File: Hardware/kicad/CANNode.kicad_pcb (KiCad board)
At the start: 4 copper layers, 66.5 x 57 mm, 58 parts, among them J1 Conn_01x04, J11 Conn_01x04, J12 Conn_01x04, J2 Conn_01x04, J21 Conn_01x04, J31 Conn_01x04, J41 Conn_01x04, J42 Conn_01x04, J43 Conn_01x04, J44 Conn_01x04, J61 Conn_02x04_Odd_Even, J81 Conn_01x10, J91 Conn_01x04, U1 Teensy3.2, U2 SN65HVD230, U21 PCA9306, U31 MAX3485, U41 MAX3485, U91 LM1117-5.0

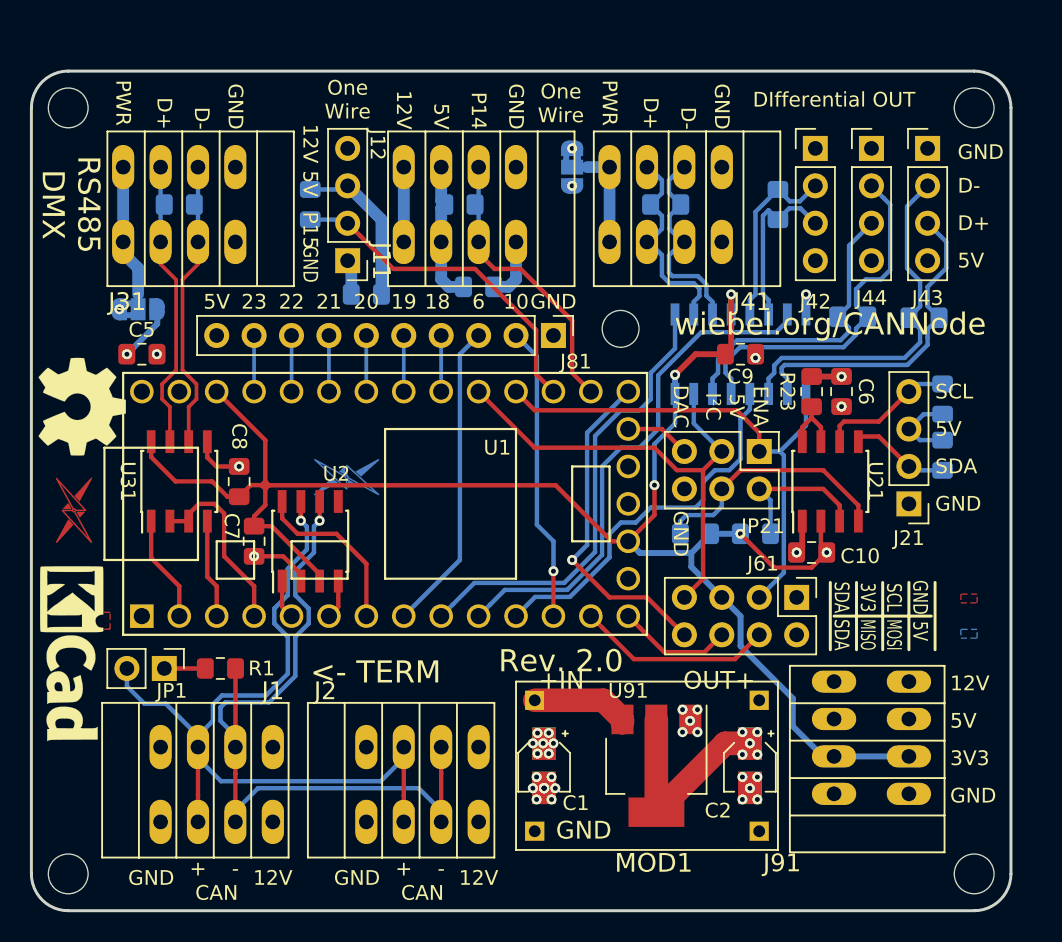
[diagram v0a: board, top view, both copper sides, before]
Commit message: second RS485 swapped with OW
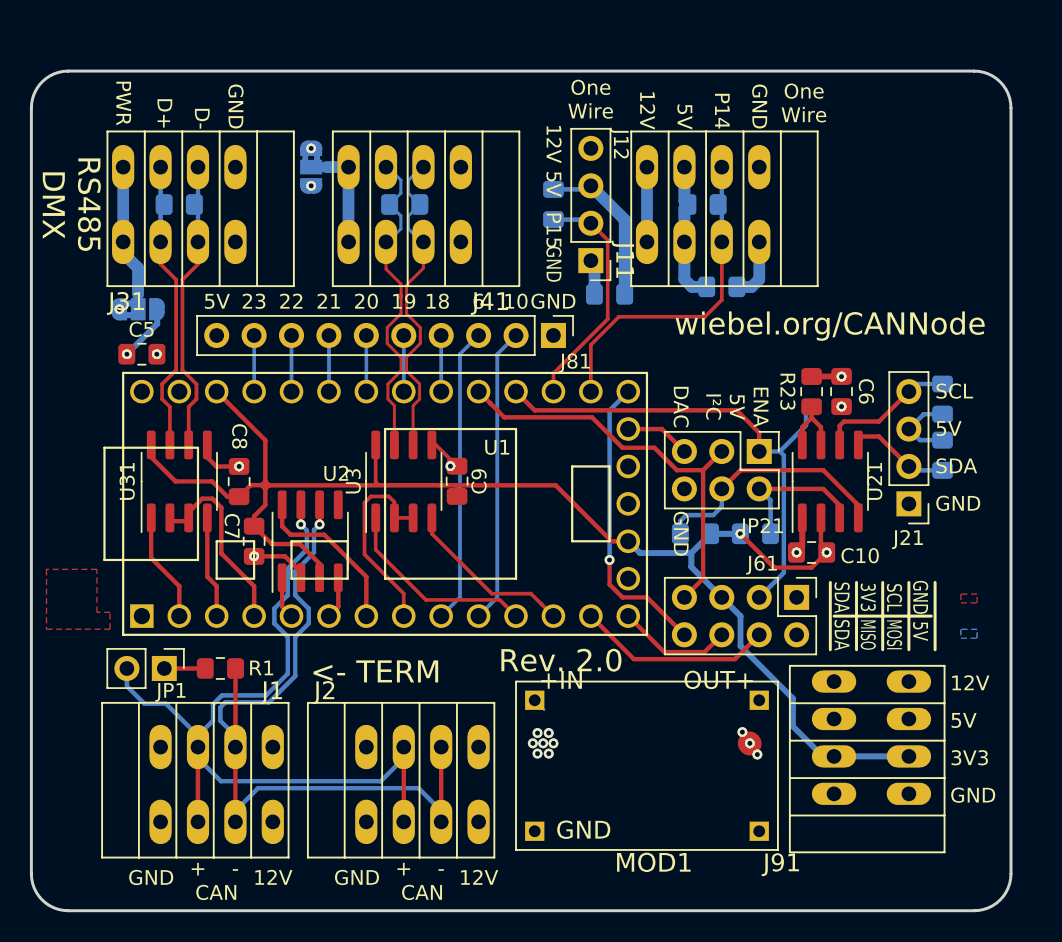
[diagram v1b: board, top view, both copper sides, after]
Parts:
- removed ? (x2): , own:LOGO_MID
- removed C1 (x2), C2 (x2): CP, Capacitor_SMD:CP_Elec_3x5.4
- removed J42, J43, J44: Conn_01x04, Connector_PinHeader_2.54mm:PinHeader_1x04_P2.54mm_Vertical
- removed R3, R4, R5: 120, Resistor_SMD:R_0805_2012Metric_Pad1.15x1.40mm_HandSolder
- removed REF** (x5): MountingHole_2.5mm, MountingHole:MountingHole_2.5mm
- removed REF**: KiCAD Logo, Symbol:Symbol_KiCAD-Logo_CopperAndSilkScreenTop
- removed REF**: OSHW-Symbol_6.7x6mm_SilkScreen, Symbol:OSHW-Symbol_6.7x6mm_SilkScreen
- removed U41: MAX3485, Package_SO:SOIC-16_3.9x9.9mm_P1.27mm
- removed U91: LM1117-5.0, Package_TO_SOT_SMD:SOT-223-3_TabPin2
- added U3: MAX3485, Package_SO:SOIC-8_3.9x4.9mm_P1.27mm, F.Cu at (94.6, 64.5)
- MOD1: value OWN_DCDC -> DSN-MINI-360
- moved C9 21.1 mm to (98.2, 64.5), turned to 90 degrees
- moved J41 17.7 mm to (90.9, 43.2)
- moved JP41 17.7 mm to (88.3, 43.2)
- moved R2 17.7 mm to (94.7, 45.7)
- moved C3 16.5 mm to (116.2, 51.3)
- moved J11 16.5 mm to (111.1, 43.2)
- moved R11 16.5 mm to (104.8, 45.7)
- moved R12 16.5 mm to (114.9, 45.7)
- moved C4 16.5 mm to (108.6, 51.8)
- moved J12 16.5 mm to (107.3, 49.5)
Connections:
- net /16 renamed /18
- net /17 renamed /19
- net /D1+ renamed /UA2+
- net /D1- renamed /UA2-
- net Net-(J12-Pad2) renamed /OW15
- J31 pad 2: /UA1+ -> /UA1-
- J31 pad 3: /UA1- -> /UA1+
- MOD1 pad IN+: +12V -> (no net)
- MOD1 pad IN-: GND -> (no net)
- MOD1 pad OUT+: +5V -> (no net)
- MOD1 pad OUT-: GND -> (no net)
- R6 pad 1: /UA1+ -> /UA1-
- R6 pad 2: /UA1- -> /UA1+
- U1 pad 10: /DI2_8 -> /10
- U1 pad 11: /EN34_9 -> Net-(U1-Pad11)
- U1 pad 12: /10 -> Net-(U1-Pad12)
- U1 pad 15: Net-(U1-Pad15) -> (no net)
- U1 pad 18: Net-(U1-Pad18) -> (no net)
- U1 pad 32: Net-(U1-Pad32) -> (no net)
- U1 pad 8: /6 -> Net-(U1-Pad8)
- U1 pad 9: /DI1_7 -> /6
- U2 pad 5: Net-(U2-Pad5) -> (no net)
- U31 pad 6: /UA1+ -> /UA1-
- U31 pad 7: /UA1- -> /UA1+
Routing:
- net /DI2_8: track 35.4 -> 0.00 mm
- net /DI1_7: track 31.4 -> 0.00 mm
- net /EN34_9: track 26.0 -> 0.00 mm
- net /D3-: track 24.9 -> 0.00 mm
- net /D4-: track 24.8 -> 0.00 mm
- net /D3+: track 22.4 -> 0.00 mm
- net /D4+: track 20.8 -> 0.00 mm
- net +5V: track 46.3 -> 31.8 mm, vias 8 -> 6
- net +3V3: track 118.5 -> 104.5 mm, vias 5 -> 2
- net Net-(U1-Pad11): track 0.00 -> 13.6 mm
- net Net-(U1-Pad8): track 0.00 -> 13.5 mm
- net /D2-: track 12.6 -> 0.00 mm
- net Net-(U1-Pad12): track 0.00 -> 11.6 mm
- net /D2+: track 11.6 -> 0.00 mm
- net /UA2+: track 14.2 -> 23.1 mm
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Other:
- board text removed: "DIfferential OUT"

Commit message: latest additions
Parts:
- moved MOD1 0.52 mm to (119.3, 89.4)
- moved C8 0.38 mm to (83.1, 64.5)
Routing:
- net Net-(U1-Pad8): track 13.5 -> 8.78 mm, vias 0 -> 1
- net +3V3: track 104.5 -> 103.4 mm
- net /UA3EN_2: track 13.0 -> 13.9 mm, vias 0 -> 1
- net /SDA0_17: track 28.4 -> 28.9 mm
- net +5V: track 31.8 -> 31.7 mm, vias 6 -> 3
- net +12V: vias 9 -> 2

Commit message: pproaching v2.5
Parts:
- removed the C5 at (76.8, 55.9)
- removed the C9 at (98.2, 64.5)
- removed J11, J91: Conn_01x04, CANNode:OWN_KF141V-P4_simple
- removed the J2 at (99.7, 87.6)
- removed J21: Conn_01x04, Connector_PinHeader_2.54mm:PinHeader_1x04_P2.54mm_Vertical
- removed JP21: Conn_02x03_Odd_Even, Connector_PinHeader_2.54mm:PinHeader_2x03_P2.54mm_Vertical
- removed R11, R12, R24, R25: 4.7k, Resistor_SMD:R_0805_2012Metric_Pad1.15x1.40mm_HandSolder
- removed the R2 at (94.7, 45.7)
- added C1: C, Capacitor_SMD:C_0805_2012Metric_Pad1.15x1.40mm_HandSolder, B.Cu at (81.2, 51.3)
- added C10: C, Capacitor_SMD:C_0805_2012Metric_Pad1.15x1.40mm_HandSolder, B.Cu at (94.6, 51.4)
- added C11: C, Capacitor_SMD:C_0805_2012Metric_Pad1.15x1.40mm_HandSolder, B.Cu at (123.8, 42.2)
- added C2: C, Capacitor_SMD:C_0805_2012Metric_Pad1.15x1.40mm_HandSolder, B.Cu at (123.8, 44.2)
- added C8: C, Capacitor_SMD:C_0805_2012Metric_Pad1.15x1.40mm_HandSolder, F.Cu at (98.3, 64.5)
- added H1: MountingHole, MountingHole:MountingHole_3.5mm, F.Cu at (72.0, 39.4)
- added H2: MountingHole, MountingHole:MountingHole_3.5mm, F.Cu at (133.2, 39.4)
- added H3: MountingHole, MountingHole:MountingHole_3.5mm, F.Cu at (72.0, 90.9)
- added H4: MountingHole, MountingHole:MountingHole_3.5mm, F.Cu at (133.2, 90.9)
- added J6: Conn_01x04, 00_mylib:WAGO_243_4-Pole, F.Cu at (131.7, 40.9)
- added J8: Conn_01x03, 00_mylib:WAGO_243_3-Pole, F.Cu at (133.7, 88.1)
- added J9: Conn_01x04, Connector_PinHeader_2.54mm:PinHeader_1x04_P2.54mm_Vertical, F.Cu at (128.9, 64.9)
- added JP4: Conn_02x03_Odd_Even, Connector_PinHeader_2.54mm:PinHeader_2x03_P2.54mm_Vertical, F.Cu at (113.7, 65.0)
- added Log1: Logo, 00_mylib:LOGO_MID, F.Cu at (73.3, 51.3)
- added Log2: Logo, Symbol:OSHW-Logo_5.7x6mm_Copper, F.Cu at (73.3, 55.6)
- added Log3: Logo, 00_mylib:LOGO_MID, B.Cu at (113.7, 55.1)
- added Log4: Logo, Symbol:OSHW-Logo_5.7x6mm_Copper, B.Cu at (105.0, 63.8)
- added R3: 120, Resistor_SMD:R_0805_2012Metric_Pad1.15x1.40mm_HandSolder, B.Cu at (94.6, 45.7)
- added R4: 4.7k, Resistor_SMD:R_0805_2012Metric_Pad1.15x1.40mm_HandSolder, B.Cu at (103.3, 45.7)
- added R5: 4.7k, Resistor_SMD:R_0805_2012Metric_Pad1.15x1.40mm_HandSolder, B.Cu at (121.0, 49.8)
- added R7: 4.7k, Resistor_SMD:R_0805_2012Metric_Pad1.15x1.40mm_HandSolder, B.Cu at (131.2, 61.6)
- added R8: 4.7k, Resistor_SMD:R_0805_2012Metric_Pad1.15x1.40mm_HandSolder, B.Cu at (131.2, 57.8)
- J1: footprint CANNode:OWN_KF141V-P4_simple -> 00_mylib:WAGO_243_4-Pole
- J2: renamed from J31; footprint CANNode:OWN_KF141V-P4_simple -> 00_mylib:OWN_KF141V-P4_simple
- J5: renamed from J41; footprint CANNode:OWN_KF141V-P4_simple -> 00_mylib:OWN_KF141V-P4_simple
- MOD1: footprint CANNode:OWN_DC-DC -> 00_mylib:OWN_DC-DC
- moved J1 11.7 mm to (74.3, 89.9)
- moved C4 9.56 mm to (101.2, 45.7), turned to 270 degrees
- moved C3 9.17 mm to (107.1, 51.8), turned to 180 degrees
- moved J7 1.52 mm to (105.8, 49.5)
- moved JP2 1.02 mm to (79.4, 77.2)
- moved R2 1.02 mm to (83.2, 77.2)
- moved J5 0.06 mm to (90.8, 43.2)
- moved JP3 0.06 mm to (88.4, 43.2)
- renumbered C6 to C5, C7 to C6, C8 to C7, C10 to C9, J81 to J3, J61 to J4, J12 to J7, JP31 to JP1, JP1 to JP2, JP41 to JP3, R6 to R1, R21 to R10, R1 to R2, R23 to R6, R22 to R9, U31 to U1, U1 to U3, U3 to U4, U21 to U5
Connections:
- net Net-(U1-Pad11) renamed /RX2
- C4 pad 1: +5V -> +12V
- MOD1 pad IN+: (no net) -> +12V
- MOD1 pad IN-: (no net) -> GND
- MOD1 pad OUT+: (no net) -> +5V
- MOD1 pad OUT-: (no net) -> GND
- U1 pad 4: /TX2 -> /TX1
- U3 pad 12: Net-(U1-Pad12) -> /TX2
- U3 pad 3: /TX2 -> /TX1
- U4 pad 4: Net-(U1-Pad12) -> /TX2
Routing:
- net +12V: track 126.6 -> 22.8 mm, vias 2 -> 4
- net /CAN-: track 55.1 -> 30.0 mm
- net /CAN+: track 56.5 -> 31.6 mm
- net +5V: track 31.7 -> 12.5 mm, vias 3 -> 2
- net /OW14: track 23.3 -> 5.87 mm
- net +3V3: track 103.4 -> 86.0 mm
- net (no net): track 0.90 -> 16.5 mm
- net /OW15: track 16.1 -> 1.92 mm
- net Net-(U1-Pad12): track 11.6 -> 0.00 mm
- net /TX1: track 0.00 -> 6.71 mm
- net Net-(C10-Pad2): track 7.62 -> 12.8 mm
- net /TX2: track 6.71 -> 11.6 mm
- net Net-(C1-Pad2): track 10.1 -> 13.6 mm
- net GND: track 19.5 -> 22.3 mm, vias 6 -> 5
- net /UA1+: track 19.9 -> 21.9 mm
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- removed copper zone on B.Cu, net (none)
- removed copper zone on F.Cu, net (none)
- removed copper zone on In1.Cu, net (none)
- removed copper zone on In2.Cu, net (none)
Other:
- board text added: "CAN_H"
- board text added: "CAN_L"
- board text added: "D P14"
- board text added: "ENABLE 5V-I²C"
- board text added: "OneWire"
- board text added: "RS485"
- board text added: "Rev. 2.5"
- board text added: "UA1"
- board text added: "UA2"
- board text added: "v2.5"
- board text removed: "+"
- board text removed: "-"
- board text removed: "CAN"
- board text removed: "ENA 5V I²C"
- board text removed: "One Wire"
- board text removed: "P14"
- board text removed: "RS485 DMX"
- board text removed: "Rev. 2.0"

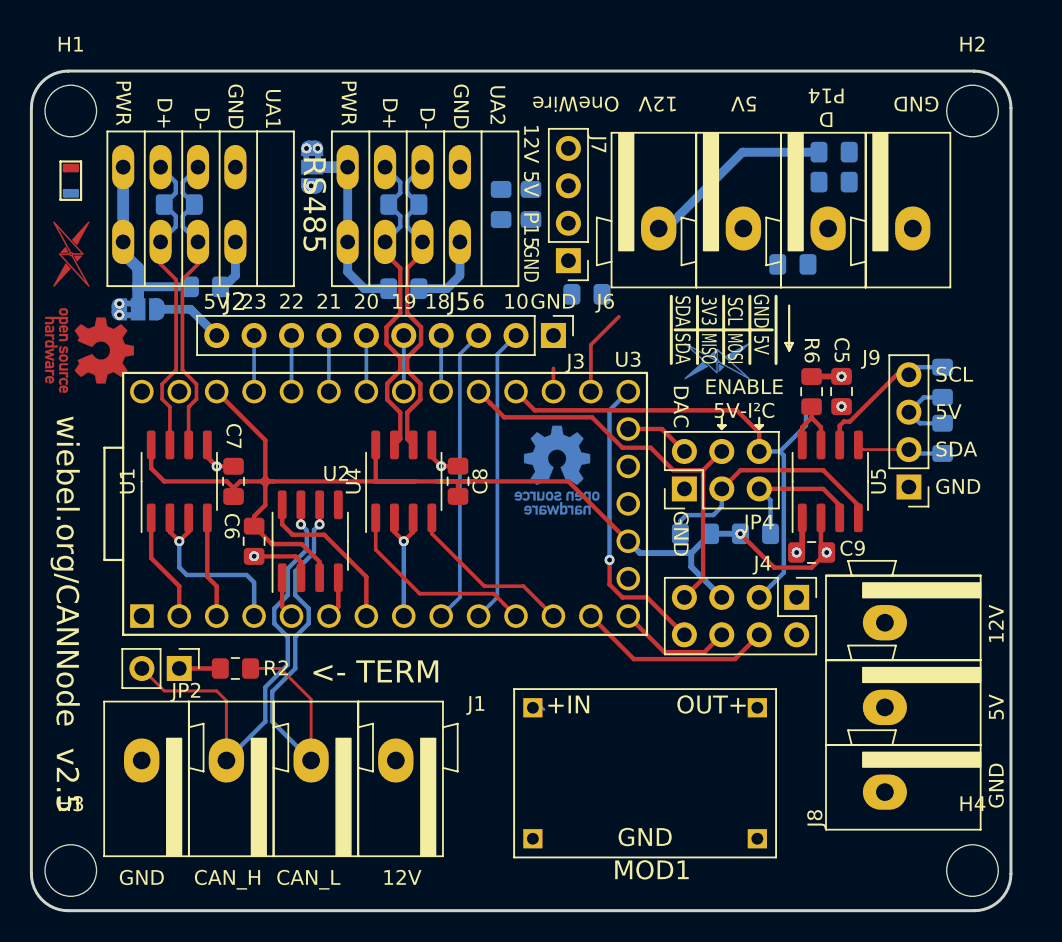
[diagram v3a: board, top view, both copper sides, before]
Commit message: PCB fixed silkscreen
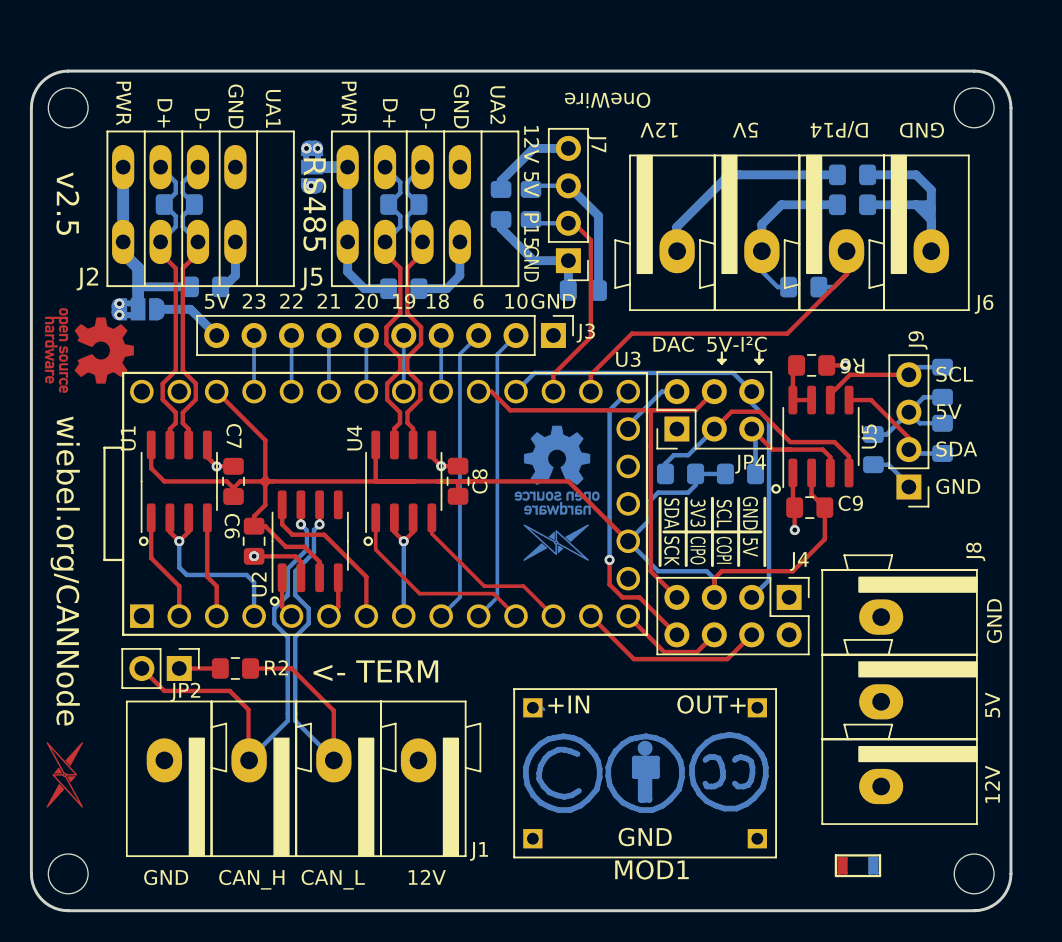
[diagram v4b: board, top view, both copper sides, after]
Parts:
- added REF**: Symbol_CC-ShareAlike_CopperTop_Small, Symbol:Symbol_CC-ShareAlike_CopperTop_Small, B.Cu at (105.4, 84.3)
- added REF**: Symbol_CC-Attribution_CopperTop_Small, Symbol:Symbol_CC-Attribution_CopperTop_Small, B.Cu at (111.0, 84.3)
- added REF**: Symbol_CreativeCommons_CopperTop_Type2_Small, Symbol:Symbol_CreativeCommons_CopperTop_Type2_Small, B.Cu at (116.8, 84.3)
- C5: moved to B.Cu
- H1, H2, H3, H4: footprint MountingHole:MountingHole_3.5mm -> MountingHole:MountingHole_2.7mm
- moved Log1 35.4 mm to (72.8, 86.7)
- moved Log3 16.5 mm to (102.7, 67.4)
- moved C5 4.50 mm to (126.5, 62.4)
- moved R10 4.19 mm to (117.5, 64.0)
- moved R9 4.19 mm to (113.4, 64.0)
- moved JP4 4.10 mm to (113.2, 61.0)
- moved U5 3.11 mm to (122.9, 61.5)
- moved C9 3.05 mm to (122.2, 66.3)
- moved C11 1.99 mm to (125.1, 43.7)
- moved C2 1.99 mm to (125.1, 45.7)
- moved J6 1.99 mm to (133.0, 42.4)
- moved R6 1.78 mm to (122.3, 56.6), turned to 0 degrees
- moved R5 1.71 mm to (121.8, 51.3)
- moved J1 1.54 mm to (75.8, 89.9)
- moved J4 0.51 mm to (120.8, 72.4)
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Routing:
- net GND: track 22.3 -> 51.6 mm, vias 5 -> 4
- net +5V: track 12.5 -> 36.5 mm
- net /OW14: track 5.87 -> 26.7 mm
- net /OW15: track 1.92 -> 16.3 mm
- net +3V3: track 86.0 -> 97.3 mm, vias 2 -> 0
- net +12V: track 22.8 -> 32.3 mm
- net (no net): track 16.5 -> 21.7 mm
- net /SCL0_16: track 34.5 -> 32.0 mm
- net /SDA: track 6.36 -> 8.58 mm
- net /SDA0_17: track 28.4 -> 30.5 mm
- net Net-(R6-Pad1): track 4.52 -> 3.75 mm
- net Net-(J4-Pad8): track 20.1 -> 19.6 mm
- net Net-(J4-Pad4): track 13.3 -> 12.8 mm
- net Net-(J4-Pad6): track 7.85 -> 7.34 mm
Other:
- board text added: "5V-I²C"
- board text added: "CIPO"
- board text added: "COPI"
- board text added: "D/P14"
- board text added: "SCK"
- board text removed: "D P14"
- board text removed: "ENABLE 5V-I²C"
- board text removed: "MISO"
- board text removed: "MOSI"
- board text removed: "Rev. 2.5"
